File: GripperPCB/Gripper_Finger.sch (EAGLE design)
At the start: 6 parts, among them IC1 ATMEGA328PB-AU

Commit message: board update with l293d
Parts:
- added IC2, IC3: L293D, st-microelectronics:L293D
- added MOTOR_POWER: 22-23-2021, con-molex:22-23-2021
- added R3: (no value), pot:TRIM_US-B64Y
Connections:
- new net N$10: IC2.VCC1, IC2.VCC2, IC3.VCC1, IC3.VCC2, MOTOR_POWER-2.S
- new net N$9: IC1G$1.(PCINT10/PTCY2/ADC2)PC2, R3.S
- net GND: now also IC2.GND1, IC2.GND2, IC2.GND3, IC2.GND4, IC3.GND1, IC3.GND2, IC3.GND3, IC3.GND4, MOTOR_POWER-1.S, R3.A
- net VCC: now also R3.E
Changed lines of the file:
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@@
 <part name="P+2" library="supply1" library_urn="urn:adsk.eagle:library:371" deviceset="VCC" device=""/>
 <part name="P+3" library="supply1" library_urn="urn:adsk.eagle:library:371" deviceset="VCC" device=""/>
+<part name="R3" library="pot" library_urn="urn:adsk.eagle:library:331" deviceset="TRIM_US-" device="B64Y" package3d_urn="urn:adsk.eagle:package:22690/1"/>
+<part name="IC2" library="st-microelectronics" library_urn="urn:adsk.eagle:library:368" deviceset="L293D" device="" package3d_urn="urn:adsk.eagle:package:26820/1"/>
+<part name="IC3" library="st-microelectronics" library_urn="urn:adsk.eagle:library:368" deviceset="L293D" device="" package3d_urn="urn:adsk.eagle:package:26820/1"/>
+<part name="GND4" library="supply1" library_urn="urn:adsk.eagle:library:371" deviceset="GND" device=""/>
+<part name="GND5" library="supply1" library_urn="urn:adsk.eagle:library:371" deviceset="GND" device=""/>
+<part name="GND6" library="supply1" library_urn="urn:adsk.eagle:library:371" deviceset="GND" device=""/>
+<part name="MOTOR_POWER" library="con-molex" library_urn="urn:adsk.eagle:library:165" deviceset="22-23-2021" device="" package3d_urn="urn:adsk.eagle:package:8078633/1"/>
+<part name="GND7" library="supply1" library_urn="urn:adsk.eagle:library:371" deviceset="GND" device=""/>
 </parts>
 <sheets>
@@
 <attribute name="VALUE" x="137.16" y="30.48" size="1.778" layer="96" rot="R90"/>
 </instance>
+<instance part="R3" gate="G$1" x="165.1" y="22.86" smashed="yes">
+<attribute name="NAME" x="160.02" y="20.32" size="1.778" layer="95" rot="R90"/>
+<attribute name="VALUE" x="162.56" y="20.32" size="1.778" layer="96" rot="R90"/>
+</instance>
+<instance part="IC2" gate="G$1" x="-27.94" y="27.94" smashed="yes">
+<attribute name="NAME" x="-38.1" y="49.276" size="1.778" layer="95"/>
+<attribute name="VALUE" x="-38.1" y="5.08" size="1.778" layer="96"/>
+</instance>
+<instance part="IC3" gate="G$1" x="-81.28" y="27.94" smashed="yes">
+<attribute name="NAME" x="-91.44" y="49.276" size="1.778" layer="95"/>
+<attribute name="VALUE" x="-91.44" y="5.08" size="1.778" layer="96"/>
+</instance>
+<instance part="GND4" gate="1" x="-111.76" y="-10.16" smashed="yes">
+<attribute name="VALUE" x="-114.3" y="-12.7" size="1.778" layer="96"/>
+</instance>
+<instance part="GND5" gate="1" x="-55.88" y="-10.16" smashed="yes">
+<attribute name="VALUE" x="-58.42" y="-12.7" size="1.778" layer="96"/>
+</instance>
+<instance part="GND6" gate="1" x="-2.54" y="-10.16" smashed="yes">
+<attribute name="VALUE" x="-5.08" y="-12.7" size="1.778" layer="96"/>
+</instance>
+<instance part="MOTOR_POWER" gate="-1" x="-101.6" y="81.28" smashed="yes" rot="R90">
+<attribute name="NAME" x="-100.838" y="83.82" size="1.524" layer="95" rot="R90"/>
+<attribute name="VALUE" x="-102.997" y="80.518" size="1.778" layer="96" rot="R90"/>
+</instance>
+<instance part="MOTOR_POWER" gate="-2" x="-99.06" y="81.28" smashed="yes" rot="R90">
+<attribute name="NAME" x="-98.298" y="83.82" size="1.524" layer="95" rot="R90"/>
+</instance>
+<instance part="GND7" gate="1" x="-104.14" y="73.66" smashed="yes">
+<attribute name="VALUE" x="-106.68" y="71.12" size="1.778" layer="96"/>
+</instance>
 </instances>
 <busses>
@@
 <wire x1="139.7" y1="5.08" x2="152.4" y2="5.08" width="0.1524" layer="91"/>
 <junction x="152.4" y="5.08"/>
+<pinref part="R3" gate="G$1" pin="A"/>
+<wire x1="152.4" y1="15.24" x2="165.1" y2="15.24" width="0.1524" layer="91"/>
+<junction x="152.4" y="15.24"/>
 </segment>
 <segment>
@@
 <pinref part="ICSP" gate="1" pin="1"/>
 <wire x1="149.86" y1="45.72" x2="147.32" y2="45.72" width="0.1524" layer="91"/>
+</segment>
+<segment>
+<pinref part="GND4" gate="1" pin="GND"/>
+<pinref part="IC3" gate="G$1" pin="GND1"/>
+<wire x1="-111.76" y1="-7.62" x2="-111.76" y2="25.4" width="0.1524" layer="91"/>
+<wire x1="-111.76" y1="25.4" x2="-111.76" y2="30.48" width="0.1524" layer="91"/>
+<wire x1="-111.76" y1="30.48" x2="-96.52" y2="30.48" width="0.1524" layer="91"/>
+<pinref part="IC3" gate="G$1" pin="GND2"/>
+<wire x1="-96.52" y1="25.4" x2="-111.76" y2="25.4" width="0.1524" layer="91"/>
+<junction x="-111.76" y="25.4"/>
+</segment>
+<segment>
+<pinref part="IC3" gate="G$1" pin="GND3"/>
+<pinref part="IC2" gate="G$1" pin="GND1"/>
+<wire x1="-66.04" y1="30.48" x2="-55.88" y2="30.48" width="0.1524" layer="91"/>
+<pinref part="IC2" gate="G$1" pin="GND2"/>
+<pinref part="IC3" gate="G$1" pin="GND4"/>
+<wire x1="-55.88" y1="30.48" x2="-43.18" y2="30.48" width="0.1524" layer="91"/>
+<wire x1="-43.18" y1="25.4" x2="-55.88" y2="25.4" width="0.1524" layer="91"/>
+<wire x1="-55.88" y1="25.4" x2="-66.04" y2="25.4" width="0.1524" layer="91"/>
+<wire x1="-55.88" y1="30.48" x2="-55.88" y2="25.4" width="0.1524" layer="91"/>
+<junction x="-55.88" y="30.48"/>
+<junction x="-55.88" y="25.4"/>
+<pinref part="GND5" gate="1" pin="GND"/>
+<wire x1="-55.88" y1="25.4" x2="-55.88" y2="-7.62" width="0.1524" layer="91"/>
+</segment>
+<segment>
+<pinref part="IC2" gate="G$1" pin="GND3"/>
+<pinref part="GND6" gate="1" pin="GND"/>
+<wire x1="-12.7" y1="30.48" x2="-2.54" y2="30.48" width="0.1524" layer="91"/>
+<wire x1="-2.54" y1="30.48" x2="-2.54" y2="25.4" width="0.1524" layer="91"/>
+<pinref part="IC2" gate="G$1" pin="GND4"/>
+<wire x1="-2.54" y1="25.4" x2="-2.54" y2="-7.62" width="0.1524" layer="91"/>
+<wire x1="-12.7" y1="25.4" x2="-2.54" y2="25.4" width="0.1524" layer="91"/>
+<junction x="-2.54" y="25.4"/>
+</segment>
+<segment>
+<pinref part="GND7" gate="1" pin="GND"/>
+<wire x1="-104.14" y1="76.2" x2="-104.14" y2="78.74" width="0.1524" layer="91"/>
+<pinref part="MOTOR_POWER" gate="-1" pin="S"/>
+<wire x1="-104.14" y1="78.74" x2="-101.6" y2="78.74" width="0.1524" layer="91"/>
 </segment>
 </net>
@@
 <wire x1="139.7" y1="30.48" x2="152.4" y2="30.48" width="0.1524" layer="91"/>
 <junction x="139.7" y="30.48"/>
+<pinref part="R3" gate="G$1" pin="E"/>
+<wire x1="165.1" y1="30.48" x2="152.4" y2="30.48" width="0.1524" layer="91"/>
+<junction x="152.4" y="30.48"/>
 </segment>
 </net>
@@
 </segment>
 </net>
+<net name="N$9" class="0">
+<segment>
+<pinref part="R3" gate="G$1" pin="S"/>
+<wire x1="170.18" y1="22.86" x2="170.18" y2="38.1" width="0.1524" layer="91"/>
+<wire x1="170.18" y1="38.1" x2="127" y2="38.1" width="0.1524" layer="91"/>
+<wire x1="127" y1="38.1" x2="127" y2="22.86" width="0.1524" layer="91"/>
+<pinref part="IC1" gate="G$1" pin="(PCINT10/PTCY2/ADC2)PC2"/>
+<wire x1="127" y1="22.86" x2="114.3" y2="22.86" width="0.1524" layer="91"/>
+</segment>
+</net>
+<net name="N$10" class="0">
+<segment>
+<pinref part="MOTOR_POWER" gate="-2" pin="S"/>
+<pinref part="IC3" gate="G$1" pin="VCC2"/>
+<wire x1="-99.06" y1="78.74" x2="-99.06" y2="50.8" width="0.1524" layer="91"/>
+<wire x1="-99.06" y1="50.8" x2="-99.06" y2="10.16" width="0.1524" layer="91"/>
+<wire x1="-99.06" y1="10.16" x2="-96.52" y2="10.16" width="0.1524" layer="91"/>
+<pinref part="IC3" gate="G$1" pin="VCC1"/>
+<wire x1="-66.04" y1="45.72" x2="-66.04" y2="50.8" width="0.1524" layer="91"/>
+<wire x1="-66.04" y1="50.8" x2="-99.06" y2="50.8" width="0.1524" layer="91"/>
+<junction x="-99.06" y="50.8"/>
+<pinref part="IC2" gate="G$1" pin="VCC1"/>
+<wire x1="-12.7" y1="45.72" x2="-12.7" y2="50.8" width="0.1524" layer="91"/>
+<wire x1="-12.7" y1="50.8" x2="-53.34" y2="50.8" width="0.1524" layer="91"/>
+<junction x="-66.04" y="50.8"/>
+<pinref part="IC2" gate="G$1" pin="VCC2"/>
+<wire x1="-53.34" y1="50.8" x2="-66.04" y2="50.8" width="0.1524" layer="91"/>
+<wire x1="-43.18" y1="10.16" x2="-53.34" y2="10.16" width="0.1524" layer="91"/>
+<wire x1="-53.34" y1="10.16" x2="-53.34" y2="50.8" width="0.1524" layer="91"/>
+<junction x="-53.34" y="50.8"/>
+</segment>
+</net>

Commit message: version 1.0.0 sent to engineering
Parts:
- added M1, M2, M3: 22-23-2021, con-molex:22-23-2021
- added R4: (no value), rcl:R-EU_0204/5
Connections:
- net N$1 renamed SCL
- net N$10 renamed MOTOR_POWER
- net N$2 renamed SDA
- net N$4 renamed SCK
- net N$5 renamed MISO
- net N$6 renamed MOSI
- net N$7 renamed LIGHT
- net N$8 renamed POT1
- net N$9 renamed POT2
- removed net N$3: IC1G$1.PC6(!RESET!/PCINT14), ICSP.2
- new net M1A: IC2.4Y, M1-1.S
- new net M1B: IC2.3Y, M1-2.S
- new net M2A: IC2.1Y, M2-2.S
- new net M2B: IC2.2Y, M2-1.S
- new net M3A: IC3.2Y, M3-1.S
- new net M3B: IC3.1Y, M3-2.S
- new net N$11: IC1G$1.PD2(INT0/OC3B/OC4B/PTCX2Y10/PCINT18), IC2.3A
- new net N$12: IC1G$1.PD3(INT1/OC2B/PTCX3Y11/PCINT19), IC2.3-4EN
- new net N$13: IC1G$1.PD4(XCK0/T0/PTCX4Y12/PCINT20), IC2.4A
- new net N$20: IC1G$1.PD5(OC0B/T1/PTCX5Y13/PCINT21), IC2.1-2EN
- new net N$21: IC1G$1.PD6(OC0A/AIN0/PTCX6Y14/PCINT22), IC2.1A
- new net N$22: IC1G$1.PD7(AIN1/PTCX7Y15/PCINT23), IC2.2A
- new net N$23: IC1G$1.(PCINT1/PTCX11Y19/OC1A)PB1, IC3.2A
- new net N$24: IC1G$1.(PCINT0/PTCX10Y18/CLKO/ICP1)PB0, IC3.1A
- new net N$25: IC1G$1.(PCINT2/PTCX12Y20/OC1B/!SS0!)PB2, IC3.1-2EN
- new net RESET: IC1G$1.PC6(!RESET!/PCINT14), ICSP.2, R4.1
- net VCC: now also R4.2

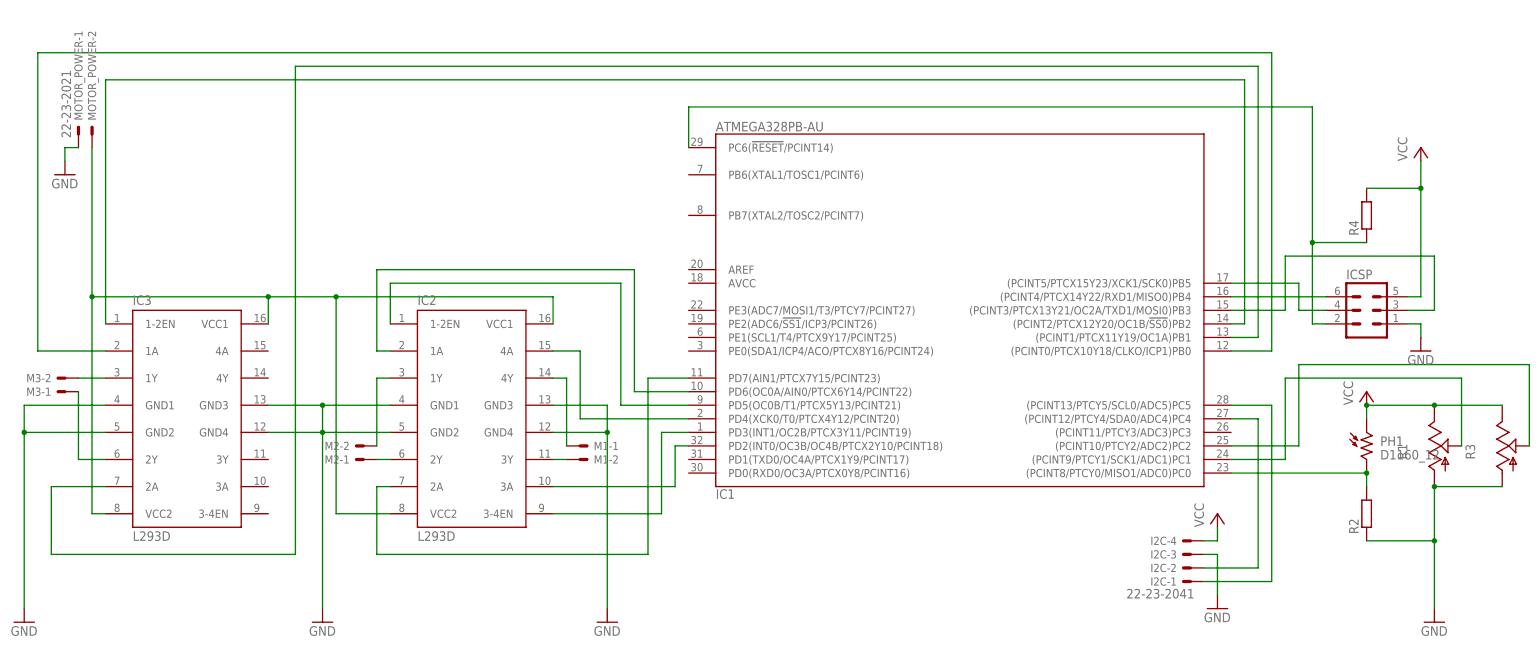
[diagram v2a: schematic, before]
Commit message: added crystal
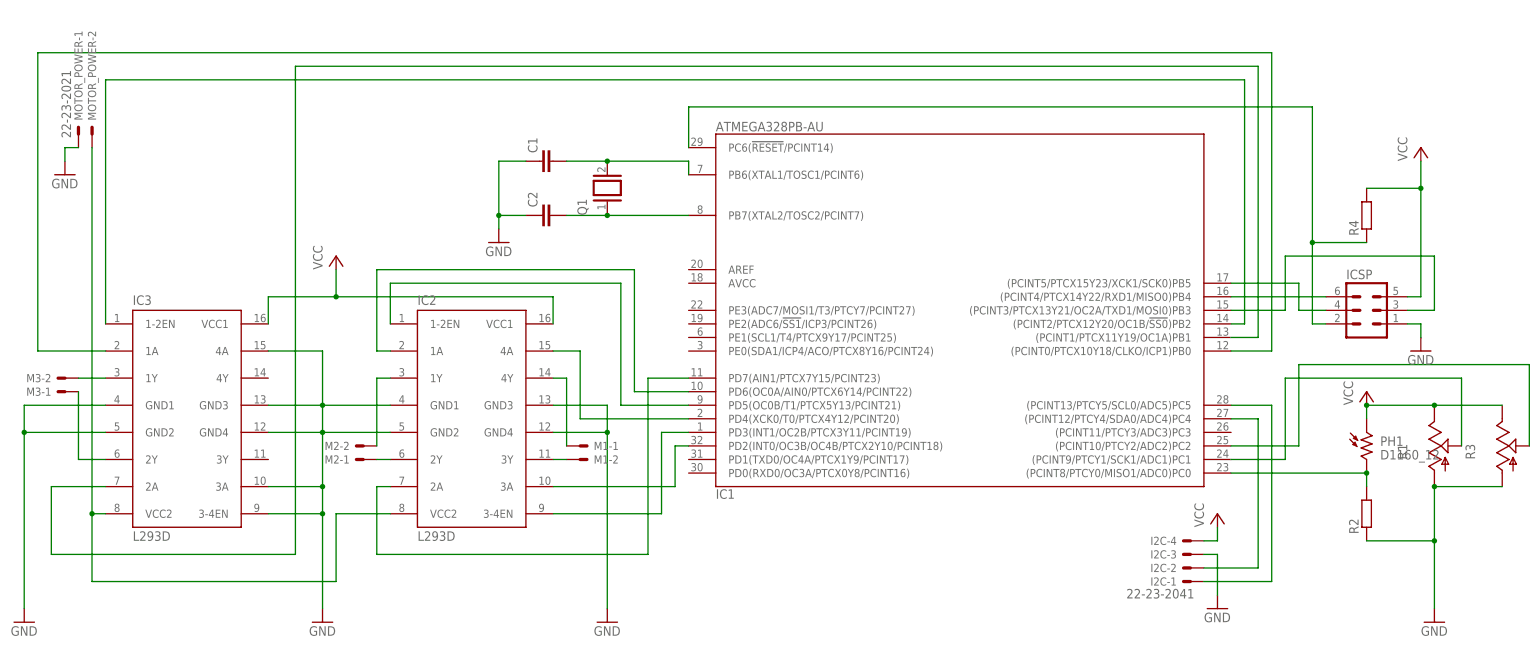
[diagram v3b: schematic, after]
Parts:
- added C1, C2: (no value), capacitor-wima:C2.5/2
- added Q1: (no value), special:XTAL/S
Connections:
- net N$11 renamed M1BSIG
- net N$12 renamed M1E
- net N$13 renamed M1ASIG
- net N$20 renamed M2E
- net N$21 renamed M2ASIG
- net N$22 renamed M2BSIG
- net N$23 renamed M3ASIG
- net N$24 renamed M3BSIG
- net N$25 renamed M3E
- new net CRYSTAL1: C2.2, IC1G$1.PB7(XTAL2/TOSC2/PCINT7), Q1.1
- new net CRYSTAL2: C1.2, IC1G$1.PB6(XTAL1/TOSC1/PCINT6), Q1.2
- net GND: now also C1.1, C2.1, IC3.3-4EN, IC3.3A, IC3.4A
- net MOTOR_POWER: no longer IC2.VCC1, IC3.VCC1
- net VCC: now also IC2.VCC1, IC3.VCC1
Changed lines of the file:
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@@
 <part name="M3" library="con-molex" library_urn="urn:adsk.eagle:library:165" deviceset="22-23-2021" device="" package3d_urn="urn:adsk.eagle:package:8078633/1"/>
 <part name="R4" library="rcl" library_urn="urn:adsk.eagle:library:334" deviceset="R-EU_" device="0204/5" package3d_urn="urn:adsk.eagle:package:23488/1"/>
+<part name="Q1" library="special" library_urn="urn:adsk.eagle:library:367" deviceset="XTAL/S" device="" package3d_urn="urn:adsk.eagle:package:26647/2"/>
+<part name="C1" library="capacitor-wima" library_urn="urn:adsk.eagle:library:116" deviceset="C" device="2.5/2" package3d_urn="urn:adsk.eagle:package:5415/1"/>
+<part name="C2" library="capacitor-wima" library_urn="urn:adsk.eagle:library:116" deviceset="C" device="2.5/2" package3d_urn="urn:adsk.eagle:package:5415/1"/>
+<part name="GND8" library="supply1" library_urn="urn:adsk.eagle:library:371" deviceset="GND" device=""/>
+<part name="P+4" library="supply1" library_urn="urn:adsk.eagle:library:371" deviceset="VCC" device=""/>
 </parts>
 <sheets>
@@
 <attribute name="NAME" x="138.2014" y="62.23" size="1.778" layer="95" rot="R90"/>
 <attribute name="VALUE" x="143.002" y="62.23" size="1.778" layer="96" rot="R90"/>
+</instance>
+<instance part="Q1" gate="G$1" x="-2.54" y="71.12" smashed="yes" rot="R90">
+<attribute name="NAME" x="-6.35" y="66.04" size="1.778" layer="95" rot="R90"/>
+<attribute name="VALUE" x="2.54" y="66.04" size="1.778" layer="96" rot="R90"/>
+</instance>
+<instance part="C1" gate="G$1" x="-15.24" y="76.2" smashed="yes" rot="R90">
+<attribute name="NAME" x="-15.621" y="77.724" size="1.778" layer="95" rot="R90"/>
+<attribute name="VALUE" x="-10.541" y="77.724" size="1.778" layer="96" rot="R90"/>
+</instance>
+<instance part="C2" gate="G$1" x="-15.24" y="66.04" smashed="yes" rot="R90">
+<attribute name="NAME" x="-15.621" y="67.564" size="1.778" layer="95" rot="R90"/>
+<attribute name="VALUE" x="-10.541" y="67.564" size="1.778" layer="96" rot="R90"/>
+</instance>
+<instance part="GND8" gate="1" x="-22.86" y="60.96" smashed="yes">
+<attribute name="VALUE" x="-25.4" y="58.42" size="1.778" layer="96"/>
+</instance>
+<instance part="P+4" gate="VCC" x="-53.34" y="58.42" smashed="yes">
+<attribute name="VALUE" x="-55.88" y="55.88" size="1.778" layer="96" rot="R90"/>
 </instance>
 </instances>
@@
 <junction x="-55.88" y="25.4"/>
 <pinref part="GND5" gate="1" pin="GND"/>
-<wire x1="-55.88" y1="25.4" x2="-55.88" y2="-7.62" width="0.1524" layer="91"/>
+<wire x1="-55.88" y1="25.4" x2="-55.88" y2="15.24" width="0.1524" layer="91"/>
+<pinref part="IC3" gate="G$1" pin="3A"/>
+<wire x1="-55.88" y1="15.24" x2="-55.88" y2="10.16" width="0.1524" layer="91"/>
+<wire x1="-55.88" y1="10.16" x2="-55.88" y2="-7.62" width="0.1524" layer="91"/>
+<wire x1="-66.04" y1="15.24" x2="-55.88" y2="15.24" width="0.1524" layer="91"/>
+<junction x="-55.88" y="15.24"/>
+<pinref part="IC3" gate="G$1" pin="4A"/>
+<wire x1="-66.04" y1="40.64" x2="-55.88" y2="40.64" width="0.1524" layer="91"/>
+<wire x1="-55.88" y1="40.64" x2="-55.88" y2="30.48" width="0.1524" layer="91"/>
+<pinref part="IC3" gate="G$1" pin="3-4EN"/>
+<wire x1="-66.04" y1="10.16" x2="-55.88" y2="10.16" width="0.1524" layer="91"/>
+<junction x="-55.88" y="10.16"/>
 </segment>
 <segment>
@@
 <pinref part="MOTOR_POWER" gate="-1" pin="S"/>
 <wire x1="-104.14" y1="78.74" x2="-101.6" y2="78.74" width="0.1524" layer="91"/>
+</segment>
+<segment>
+<pinref part="GND8" gate="1" pin="GND"/>
+<wire x1="-22.86" y1="63.5" x2="-22.86" y2="66.04" width="0.1524" layer="91"/>
+<pinref part="C2" gate="G$1" pin="1"/>
+<wire x1="-22.86" y1="66.04" x2="-17.78" y2="66.04" width="0.1524" layer="91"/>
+<pinref part="C1" gate="G$1" pin="1"/>
+<wire x1="-22.86" y1="66.04" x2="-22.86" y2="76.2" width="0.1524" layer="91"/>
+<wire x1="-22.86" y1="76.2" x2="-17.78" y2="76.2" width="0.1524" layer="91"/>
+<junction x="-22.86" y="66.04"/>
 </segment>
 </net>
@@
 <wire x1="165.1" y1="30.48" x2="152.4" y2="30.48" width="0.1524" layer="91"/>
 <junction x="152.4" y="30.48"/>
+</segment>
+<segment>
+<pinref part="IC3" gate="G$1" pin="VCC1"/>
+<wire x1="-66.04" y1="45.72" x2="-66.04" y2="50.8" width="0.1524" layer="91"/>
+<pinref part="IC2" gate="G$1" pin="VCC1"/>
+<wire x1="-12.7" y1="45.72" x2="-12.7" y2="50.8" width="0.1524" layer="91"/>
+<wire x1="-12.7" y1="50.8" x2="-53.34" y2="50.8" width="0.1524" layer="91"/>
+<pinref part="P+4" gate="VCC" pin="VCC"/>
+<wire x1="-53.34" y1="50.8" x2="-66.04" y2="50.8" width="0.1524" layer="91"/>
+<wire x1="-53.34" y1="55.88" x2="-53.34" y2="50.8" width="0.1524" layer="91"/>
+<junction x="-53.34" y="50.8"/>
 </segment>
 </net>
@@
 </segment>
 </net>
-<net name="MOTOR_POWER" class="1">
-<segment>
-<pinref part="MOTOR_POWER" gate="-2" pin="S"/>
-<pinref part="IC3" gate="G$1" pin="VCC2"/>
-<wire x1="-99.06" y1="78.74" x2="-99.06" y2="50.8" width="0.1524" layer="91"/>
-<wire x1="-99.06" y1="50.8" x2="-99.06" y2="10.16" width="0.1524" layer="91"/>
-<wire x1="-99.06" y1="10.16" x2="-96.52" y2="10.16" width="0.1524" layer="91"/>
-<pinref part="IC3" gate="G$1" pin="VCC1"/>
-<wire x1="-66.04" y1="45.72" x2="-66.04" y2="50.8" width="0.1524" layer="91"/>
-<wire x1="-66.04" y1="50.8" x2="-99.06" y2="50.8" width="0.1524" layer="91"/>
-<junction x="-99.06" y="50.8"/>
-<pinref part="IC2" gate="G$1" pin="VCC1"/>
-<wire x1="-12.7" y1="45.72" x2="-12.7" y2="50.8" width="0.1524" layer="91"/>
-<wire x1="-12.7" y1="50.8" x2="-53.34" y2="50.8" width="0.1524" layer="91"/>
-<junction x="-66.04" y="50.8"/>
-<pinref part="IC2" gate="G$1" pin="VCC2"/>
-<wire x1="-53.34" y1="50.8" x2="-66.04" y2="50.8" width="0.1524" layer="91"/>
-<wire x1="-43.18" y1="10.16" x2="-53.34" y2="10.16" width="0.1524" layer="91"/>
-<wire x1="-53.34" y1="10.16" x2="-53.34" y2="50.8" width="0.1524" layer="91"/>
-<junction x="-53.34" y="50.8"/>
-</segment>
-</net>
-<net name="N$11" class="0">
+<net name="M1BSIG" class="0">
 <segment>
 <pinref part="IC1" gate="G$1" pin="PD2(INT0/OC3B/OC4B/PTCX2Y10/PCINT18)"/>
@@
 </segment>
 </net>
-<net name="N$12" class="0">
+<net name="M1E" class="0">
 <segment>
 <pinref part="IC1" gate="G$1" pin="PD3(INT1/OC2B/PTCX3Y11/PCINT19)"/>
@@
 </segment>
 </net>
-<net name="N$13" class="0">
+<net name="M1ASIG" class="0">
 <segment>
 <pinref part="IC1" gate="G$1" pin="PD4(XCK0/T0/PTCX4Y12/PCINT20)"/>
@@
 </segment>
 </net>
-<net name="N$20" class="0">
+<net name="M2E" class="0">
 <segment>
 <pinref part="IC1" gate="G$1" pin="PD5(OC0B/T1/PTCX5Y13/PCINT21)"/>
@@
 </segment>
 </net>
-<net name="N$21" class="0">
+<net name="M2ASIG" class="0">
 <segment>
 <pinref part="IC1" gate="G$1" pin="PD6(OC0A/AIN0/PTCX6Y14/PCINT22)"/>
@@
 </segment>
 </net>
-<net name="N$22" class="0">
+<net name="M2BSIG" class="0">
 <segment>
 <pinref part="IC1" gate="G$1" pin="PD7(AIN1/PTCX7Y15/PCINT23)"/>
@@
 </segment>
 </net>
-<net name="N$23" class="0">
+<net name="M3ASIG" class="0">
 <segment>
 <pinref part="IC1" gate="G$1" pin="(PCINT1/PTCX11Y19/OC1A)PB1"/>
@@
 </segment>
 </net>
-<net name="N$24" class="0">
+<net name="M3BSIG" class="0">
 <segment>
 <wire x1="-109.22" y1="96.52" x2="121.92" y2="96.52" width="0.1524" layer="91"/>
@@
 </segment>
 </net>
-<net name="N$25" class="0">
+<net name="M3E" class="0">
 <segment>
 <pinref part="IC3" gate="G$1" pin="1-2EN"/>
@@
 </segment>
 </net>
+<net name="CRYSTAL2" class="0">
+<segment>
+<pinref part="Q1" gate="G$1" pin="2"/>
+<pinref part="IC1" gate="G$1" pin="PB6(XTAL1/TOSC1/PCINT6)"/>
+<wire x1="-2.54" y1="76.2" x2="12.7" y2="76.2" width="0.1524" layer="91"/>
+<wire x1="12.7" y1="76.2" x2="12.7" y2="73.66" width="0.1524" layer="91"/>
+<pinref part="C1" gate="G$1" pin="2"/>
+<wire x1="-2.54" y1="76.2" x2="-10.16" y2="76.2" width="0.1524" layer="91"/>
+<junction x="-2.54" y="76.2"/>
+</segment>
+</net>
+<net name="CRYSTAL1" class="0">
+<segment>
+<pinref part="Q1" gate="G$1" pin="1"/>
+<pinref part="IC1" gate="G$1" pin="PB7(XTAL2/TOSC2/PCINT7)"/>
+<wire x1="-2.54" y1="66.04" x2="12.7" y2="66.04" width="0.1524" layer="91"/>
+<pinref part="C2" gate="G$1" pin="2"/>
+<wire x1="-10.16" y1="66.04" x2="-2.54" y2="66.04" width="0.1524" layer="91"/>
+<junction x="-2.54" y="66.04"/>
+</segment>
+</net>
+<net name="MOTOR_POWER" class="1">
+<segment>
+<pinref part="IC2" gate="G$1" pin="VCC2"/>
+<wire x1="-43.18" y1="10.16" x2="-53.34" y2="10.16" width="0.1524" layer="91"/>
+<wire x1="-53.34" y1="10.16" x2="-53.34" y2="-2.54" width="0.1524" layer="91"/>
+<wire x1="-53.34" y1="-2.54" x2="-99.06" y2="-2.54" width="0.1524" layer="91"/>
+<pinref part="IC3" gate="G$1" pin="VCC2"/>
+<wire x1="-99.06" y1="10.16" x2="-96.52" y2="10.16" width="0.1524" layer="91"/>
+<pinref part="MOTOR_POWER" gate="-2" pin="S"/>
+<wire x1="-99.06" y1="10.16" x2="-99.06" y2="78.74" width="0.1524" layer="91"/>
+<wire x1="-99.06" y1="-2.54" x2="-99.06" y2="10.16" width="0.1524" layer="91"/>
+<junction x="-99.06" y="10.16"/>
+</segment>
+</net>
